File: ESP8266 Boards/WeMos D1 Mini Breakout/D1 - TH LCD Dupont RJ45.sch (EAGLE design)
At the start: 17 parts, among them J1 RJ45-8X, Q1 2N7000, Q2 2N7000

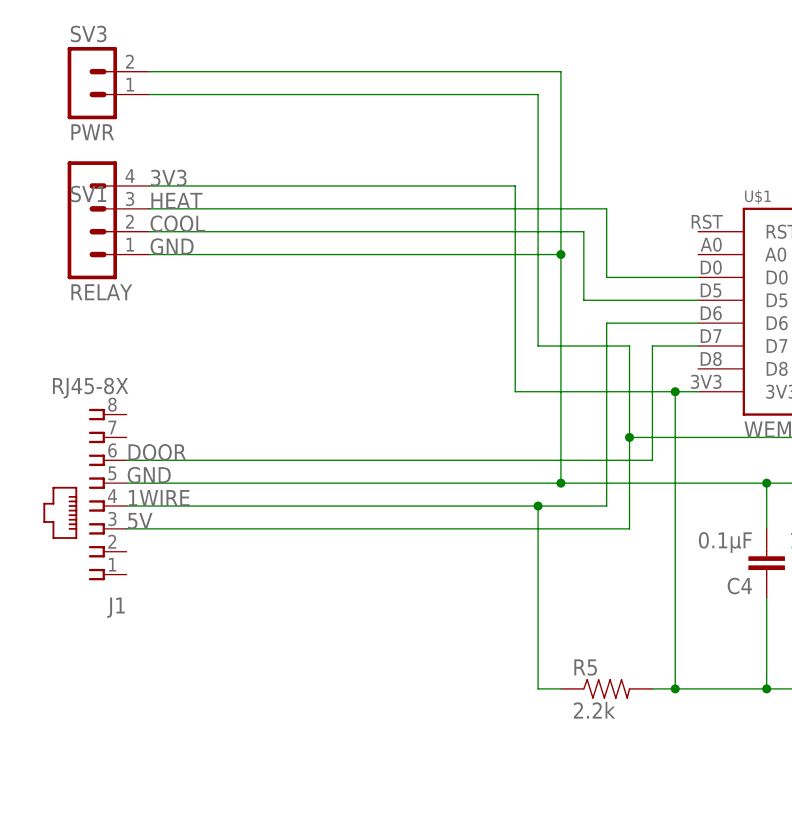
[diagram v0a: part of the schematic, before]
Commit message: Add voltage select header
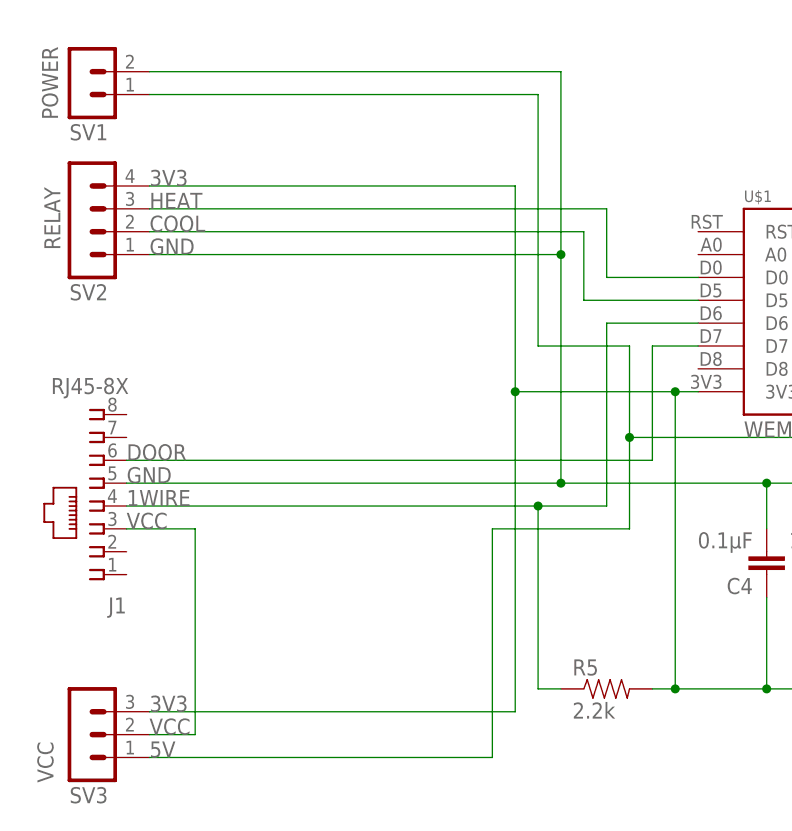
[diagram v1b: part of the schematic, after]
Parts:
- added VCC: SV3, con-lstb:MA03-1
- POWER: value PWR -> SV1
- RELAY: value RELAY -> SV2
- renumbered SV1 to RELAY, SV3 to POWER
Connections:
- new net VCC: J1.3, VCC.2
- net 3V3: now also VCC.3
- net 5V: now also VCC.1; no longer J1.3
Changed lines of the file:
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@@
 <?xml version="1.0" encoding="utf-8"?>
 <!DOCTYPE eagle SYSTEM "eagle.dtd">
-<eagle version="9.5.2">
+<eagle version="9.6.2">
 <drawing>
 <settings>
@@
 <part name="J1" library="con-tycoelectronics" deviceset="RJ45" device="" technology="-8X"/>
 <part name="R5" library="SparkFun-Resistors" library_urn="urn:adsk.eagle:library:532" deviceset="10KOHM" device="-HORIZ-1/4W-1%" package3d_urn="urn:adsk.eagle:package:39658/1" value="2.2k"/>
-<part name="SV1" library="Donnie" deviceset="HDR-4" device="" value="RELAY"/>
+<part name="RELAY" library="Donnie" deviceset="HDR-4" device="" value="SV2"/>
 <part name="SV2" library="Donnie" deviceset="HDR-4" device="" value="LCD"/>
 <part name="R3" library="SparkFun-Resistors" library_urn="urn:adsk.eagle:library:532" deviceset="10KOHM" device="-HORIZ-1/4W-1%" package3d_urn="urn:adsk.eagle:package:39658/1" value="10k"/>
@@
 <part name="C3" library="Donnie" deviceset="CAP_CERAMIC_2.54" device="" value="1.0μF"/>
 <part name="C2" library="Donnie" deviceset="CAP_CERAMIC_2.54" device="" value="0.1μF"/>
-<part name="SV3" library="Donnie" deviceset="HDR-2" device="" value="PWR"/>
+<part name="POWER" library="Donnie" deviceset="HDR-2" device="" value="SV1"/>
 <part name="FRAME1" library="frames" library_urn="urn:adsk.eagle:library:229" deviceset="LETTER_L" device="" value=" "/>
+<part name="VCC" library="con-lstb" library_urn="urn:adsk.eagle:library:162" deviceset="MA03-1" device="" package3d_urn="urn:adsk.eagle:package:8339/1" value="SV3"/>
 </parts>
 <sheets>
@@
 <attribute name="VALUE" x="92.71" y="65.278" size="1.778" layer="96"/>
 </instance>
-<instance part="SV1" gate="1" x="38.1" y="116.84" smashed="yes">
+<instance part="RELAY" gate="1" x="38.1" y="116.84" smashed="yes">
 <attribute name="VALUE" x="36.83" y="111.76" size="1.778" layer="96"/>
-<attribute name="NAME" x="36.83" y="122.682" size="1.778" layer="95"/>
+<attribute name="NAME" x="35.814" y="117.348" size="1.778" layer="95" rot="R90"/>
 </instance>
 <instance part="SV2" gate="1" x="215.9" y="78.74" smashed="yes" rot="R180">
@@
 <attribute name="VALUE" x="133.096" y="85.979" size="1.778" layer="96" font="vector" rot="R180"/>
 </instance>
-<instance part="SV3" gate="G$1" x="38.1" y="134.62" smashed="yes">
+<instance part="POWER" gate="G$1" x="38.1" y="134.62" smashed="yes">
 <attribute name="VALUE" x="36.83" y="129.54" size="1.778" layer="96"/>
-<attribute name="NAME" x="36.83" y="140.462" size="1.778" layer="95"/>
+<attribute name="NAME" x="35.56" y="131.826" size="1.778" layer="95" rot="R90"/>
 </instance>
 <instance part="FRAME1" gate="G$1" x="0" y="0" smashed="yes"/>
@@
 <attribute name="SHEET" x="233.68" y="1.27" size="2.54" layer="94"/>
 <attribute name="DRAWING_NAME" x="165.1" y="19.05" size="2.54" layer="94"/>
+</instance>
+<instance part="VCC" gate="G$1" x="38.1" y="63.5" smashed="yes">
+<attribute name="VALUE" x="36.83" y="55.88" size="1.778" layer="96"/>
+<attribute name="NAME" x="35.052" y="58.166" size="1.778" layer="95" rot="R90"/>
 </instance>
 </instances>
@@
 <wire x1="198.12" y1="91.44" x2="170.18" y2="91.44" width="0.1524" layer="91"/>
 <wire x1="149.86" y1="91.44" x2="139.7" y2="91.44" width="0.1524" layer="91"/>
-<pinref part="SV1" gate="1" pin="1"/>
+<pinref part="RELAY" gate="1" pin="1"/>
 <wire x1="45.72" y1="116.84" x2="91.44" y2="116.84" width="0.1524" layer="91"/>
 <pinref part="SV2" gate="1" pin="1"/>
@@
 <wire x1="149.86" y1="73.66" x2="149.86" y2="91.44" width="0.1524" layer="91"/>
 <junction x="149.86" y="91.44"/>
-<pinref part="SV3" gate="G$1" pin="2"/>
+<pinref part="POWER" gate="G$1" pin="2"/>
 <wire x1="45.72" y1="137.16" x2="91.44" y2="137.16" width="0.1524" layer="91"/>
 <wire x1="91.44" y1="137.16" x2="91.44" y2="116.84" width="0.1524" layer="91"/>
@@
 <label x="200.66" y="76.2" size="1.778" layer="95"/>
 <label x="165.1" y="66.04" size="1.778" layer="95" align="bottom-right"/>
-<pinref part="J1" gate="G$1" pin="3"/>
-<wire x1="43.18" y1="86.36" x2="99.06" y2="86.36" width="0.1524" layer="91"/>
-<label x="43.18" y="86.36" size="1.778" layer="95"/>
 <pinref part="C2" gate="G$1" pin="2"/>
+<wire x1="83.82" y1="86.36" x2="99.06" y2="86.36" width="0.1524" layer="91"/>
 <wire x1="134.62" y1="86.36" x2="134.62" y2="96.52" width="0.1524" layer="91"/>
-<pinref part="SV3" gate="G$1" pin="1"/>
+<pinref part="POWER" gate="G$1" pin="1"/>
 <wire x1="88.9" y1="134.62" x2="45.72" y2="134.62" width="0.1524" layer="91"/>
+<wire x1="83.82" y1="86.36" x2="83.82" y2="60.96" width="0.1524" layer="91"/>
+<pinref part="VCC" gate="G$1" pin="1"/>
+<wire x1="83.82" y1="60.96" x2="45.72" y2="60.96" width="0.1524" layer="91"/>
+<label x="45.72" y="60.96" size="1.778" layer="95"/>
 </segment>
 </net>
@@
 <junction x="104.14" y="101.6"/>
 <wire x1="86.36" y1="101.6" x2="86.36" y2="124.46" width="0.1524" layer="91"/>
-<pinref part="SV1" gate="1" pin="4"/>
+<pinref part="RELAY" gate="1" pin="4"/>
 <wire x1="86.36" y1="124.46" x2="45.72" y2="124.46" width="0.1524" layer="91"/>
 <label x="45.72" y="124.46" size="1.778" layer="95"/>
+<junction x="86.36" y="101.6"/>
+<pinref part="VCC" gate="G$1" pin="3"/>
+<wire x1="86.36" y1="66.04" x2="86.36" y2="101.6" width="0.1524" layer="91"/>
+<wire x1="45.72" y1="66.04" x2="86.36" y2="66.04" width="0.1524" layer="91"/>
+<label x="45.72" y="66.04" size="1.778" layer="95"/>
 </segment>
 </net>
@@
 <net name="COOL" class="0">
 <segment>
-<pinref part="SV1" gate="1" pin="2"/>
+<pinref part="RELAY" gate="1" pin="2"/>
 <wire x1="45.72" y1="119.38" x2="93.98" y2="119.38" width="0.1524" layer="91"/>
 <wire x1="93.98" y1="119.38" x2="93.98" y2="111.76" width="0.1524" layer="91"/>
@@
 <net name="HEAT" class="0">
 <segment>
-<pinref part="SV1" gate="1" pin="3"/>
+<pinref part="RELAY" gate="1" pin="3"/>
 <wire x1="45.72" y1="121.92" x2="96.52" y2="121.92" width="0.1524" layer="91"/>
 <wire x1="96.52" y1="121.92" x2="96.52" y2="114.3" width="0.1524" layer="91"/>
@@
 </segment>
 </net>
+<net name="VCC" class="0">
+<segment>
+<pinref part="J1" gate="G$1" pin="3"/>
+<wire x1="43.18" y1="86.36" x2="50.8" y2="86.36" width="0.1524" layer="91"/>
+<wire x1="50.8" y1="86.36" x2="50.8" y2="63.5" width="0.1524" layer="91"/>
+<pinref part="VCC" gate="G$1" pin="2"/>
+<wire x1="50.8" y1="63.5" x2="45.72" y2="63.5" width="0.1524" layer="91"/>
+<label x="43.18" y="86.36" size="1.778" layer="95"/>
+<label x="45.72" y="63.5" size="1.778" layer="95"/>
+</segment>
+</net>

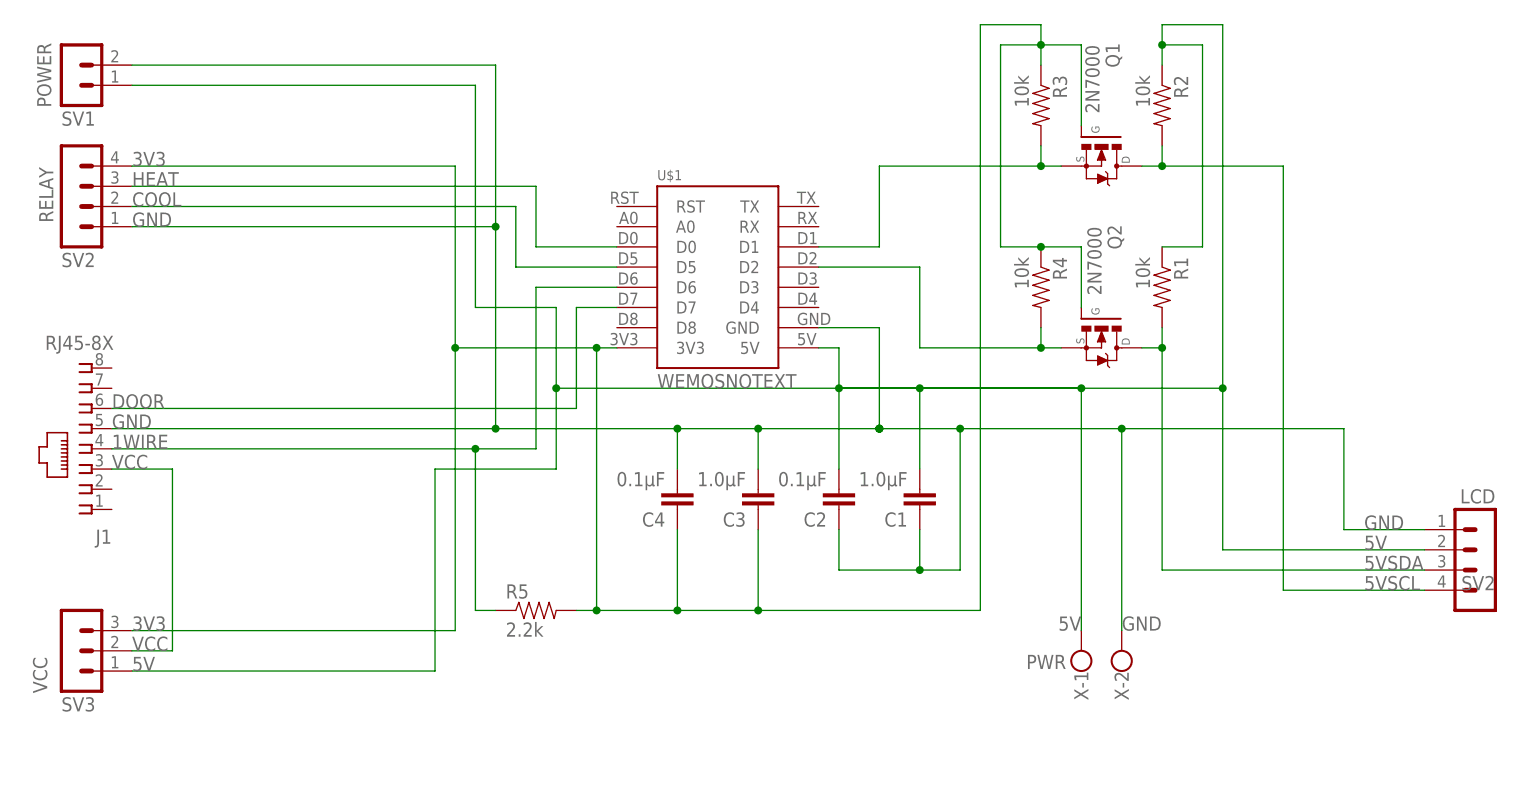
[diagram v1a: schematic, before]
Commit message: Fix pour and links
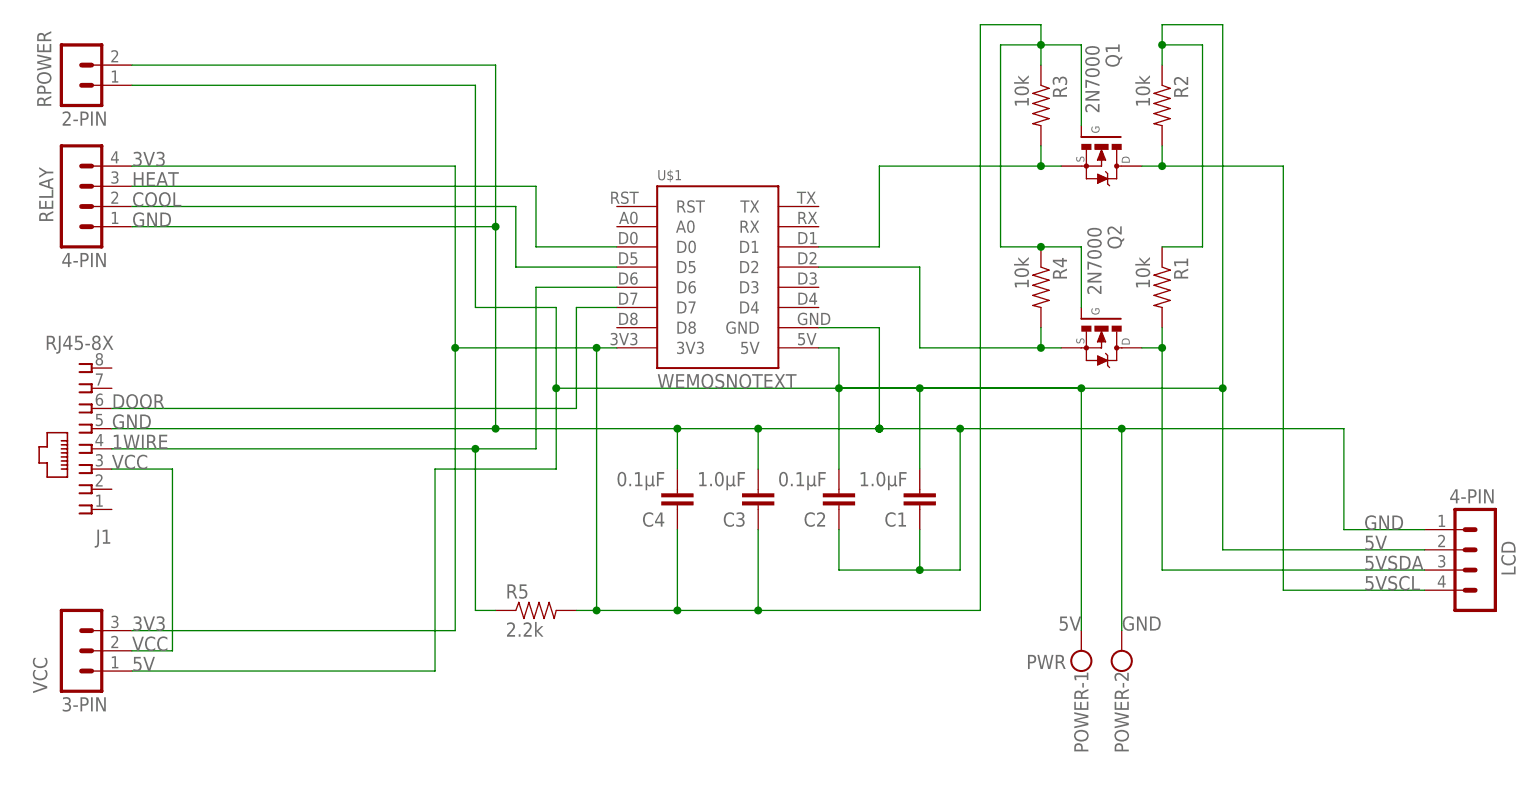
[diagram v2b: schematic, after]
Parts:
- removed X: PWR, con-wago-500:W237-102
- added RPOWER: 2-PIN, Donnie:HDR-2
- LCD: value LCD -> 4-PIN
- POWER: value SV1 -> PWR; device Donnie:HDR-2 -> con-wago-500:W237-102
- RELAY: value SV2 -> 4-PIN
- VCC: value SV3 -> 3-PIN
- renumbered SV2 to LCD
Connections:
- net 5V: now also POWER-1.KL, RPOWER.1; no longer POWER.1, X-1.KL
- net GND: now also POWER-2.KL, RPOWER.2; no longer POWER.2, X-2.KL
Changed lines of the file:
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@@
 <parts>
 <part name="U$1" library="Wemos" deviceset="WEMOS" device="NOTEXT"/>
-<part name="X" library="con-wago-500" deviceset="W237-102" device="" value="PWR"/>
+<part name="POWER" library="con-wago-500" deviceset="W237-102" device="" value="PWR"/>
 <part name="J1" library="con-tycoelectronics" deviceset="RJ45" device="" technology="-8X"/>
 <part name="R5" library="SparkFun-Resistors" library_urn="urn:adsk.eagle:library:532" deviceset="10KOHM" device="-HORIZ-1/4W-1%" package3d_urn="urn:adsk.eagle:package:39658/1" value="2.2k"/>
-<part name="RELAY" library="Donnie" deviceset="HDR-4" device="" value="SV2"/>
-<part name="SV2" library="Donnie" deviceset="HDR-4" device="" value="LCD"/>
+<part name="RELAY" library="Donnie" deviceset="HDR-4" device="" value="4-PIN"/>
+<part name="LCD" library="Donnie" deviceset="HDR-4" device="" value="4-PIN"/>
 <part name="R3" library="SparkFun-Resistors" library_urn="urn:adsk.eagle:library:532" deviceset="10KOHM" device="-HORIZ-1/4W-1%" package3d_urn="urn:adsk.eagle:package:39658/1" value="10k"/>
 <part name="R2" library="SparkFun-Resistors" library_urn="urn:adsk.eagle:library:532" deviceset="10KOHM" device="-HORIZ-1/4W-1%" package3d_urn="urn:adsk.eagle:package:39658/1" value="10k"/>
@@
 <part name="C3" library="Donnie" deviceset="CAP_CERAMIC_2.54" device="" value="1.0μF"/>
 <part name="C2" library="Donnie" deviceset="CAP_CERAMIC_2.54" device="" value="0.1μF"/>
-<part name="POWER" library="Donnie" deviceset="HDR-2" device="" value="SV1"/>
+<part name="RPOWER" library="Donnie" deviceset="HDR-2" device="" value="2-PIN"/>
 <part name="FRAME1" library="frames" library_urn="urn:adsk.eagle:library:229" deviceset="LETTER_L" device="" value=" "/>
-<part name="VCC" library="con-lstb" library_urn="urn:adsk.eagle:library:162" deviceset="MA03-1" device="" package3d_urn="urn:adsk.eagle:package:8339/1" value="SV3"/>
+<part name="VCC" library="con-lstb" library_urn="urn:adsk.eagle:library:162" deviceset="MA03-1" device="" package3d_urn="urn:adsk.eagle:package:8339/1" value="3-PIN"/>
 </parts>
 <sheets>
@@
 <attribute name="VALUE" x="111.76" y="96.52" size="1.778" layer="96"/>
 </instance>
-<instance part="X" gate="-1" x="165.1" y="60.96" smashed="yes" rot="R90">
+<instance part="POWER" gate="-1" x="165.1" y="60.96" smashed="yes" rot="R90">
 <attribute name="NAME" x="164.211" y="60.96" size="1.778" layer="95" rot="R270"/>
 </instance>
-<instance part="X" gate="-2" x="170.18" y="60.96" smashed="yes" rot="R90">
+<instance part="POWER" gate="-2" x="170.18" y="60.96" smashed="yes" rot="R90">
 <attribute name="VALUE" x="163.195" y="62.992" size="1.778" layer="96" rot="R180"/>
 <attribute name="NAME" x="169.291" y="60.96" size="1.778" layer="95" rot="R270"/>
@@
 <attribute name="NAME" x="35.814" y="117.348" size="1.778" layer="95" rot="R90"/>
 </instance>
-<instance part="SV2" gate="1" x="215.9" y="78.74" smashed="yes" rot="R180">
+<instance part="LCD" gate="1" x="215.9" y="78.74" smashed="yes" rot="R180">
 <attribute name="VALUE" x="217.17" y="83.82" size="1.778" layer="96" rot="R180"/>
-<attribute name="NAME" x="217.17" y="72.898" size="1.778" layer="95" rot="R180"/>
+<attribute name="NAME" x="219.71" y="72.898" size="1.778" layer="95" rot="R90"/>
 </instance>
 <instance part="R3" gate="G$1" x="160.02" y="132.08" smashed="yes" rot="R270">
@@
 <attribute name="VALUE" x="133.096" y="85.979" size="1.778" layer="96" font="vector" rot="R180"/>
 </instance>
-<instance part="POWER" gate="G$1" x="38.1" y="134.62" smashed="yes">
+<instance part="RPOWER" gate="G$1" x="38.1" y="134.62" smashed="yes">
 <attribute name="VALUE" x="36.83" y="129.54" size="1.778" layer="96"/>
 <attribute name="NAME" x="35.56" y="131.826" size="1.778" layer="95" rot="R90"/>
@@
 <pinref part="U$1" gate="G$1" pin="GND"/>
 <wire x1="132.08" y1="104.14" x2="139.7" y2="104.14" width="0.1524" layer="91"/>
-<pinref part="X" gate="-2" pin="KL"/>
+<pinref part="POWER" gate="-2" pin="KL"/>
 <wire x1="170.18" y1="66.04" x2="170.18" y2="91.44" width="0.1524" layer="91"/>
 <junction x="170.18" y="91.44"/>
@@
 <pinref part="RELAY" gate="1" pin="1"/>
 <wire x1="45.72" y1="116.84" x2="91.44" y2="116.84" width="0.1524" layer="91"/>
-<pinref part="SV2" gate="1" pin="1"/>
+<pinref part="LCD" gate="1" pin="1"/>
 <pinref part="C1" gate="G$1" pin="1"/>
 <junction x="139.7" y="91.44"/>
@@
 <wire x1="149.86" y1="73.66" x2="149.86" y2="91.44" width="0.1524" layer="91"/>
 <junction x="149.86" y="91.44"/>
-<pinref part="POWER" gate="G$1" pin="2"/>
+<pinref part="RPOWER" gate="G$1" pin="2"/>
 <wire x1="45.72" y1="137.16" x2="91.44" y2="137.16" width="0.1524" layer="91"/>
 <wire x1="91.44" y1="137.16" x2="91.44" y2="116.84" width="0.1524" layer="91"/>
@@
 <wire x1="134.62" y1="101.6" x2="134.62" y2="96.52" width="0.1524" layer="91"/>
 <wire x1="134.62" y1="96.52" x2="165.1" y2="96.52" width="0.1524" layer="91"/>
-<pinref part="X" gate="-1" pin="KL"/>
+<pinref part="POWER" gate="-1" pin="KL"/>
 <wire x1="165.1" y1="66.04" x2="165.1" y2="96.52" width="0.1524" layer="91"/>
 <wire x1="165.1" y1="96.52" x2="144.78" y2="96.52" width="0.1524" layer="91"/>
@@
 <wire x1="182.88" y1="76.2" x2="182.88" y2="96.52" width="0.1524" layer="91"/>
 <wire x1="88.9" y1="106.68" x2="88.9" y2="134.62" width="0.1524" layer="91"/>
-<pinref part="SV2" gate="1" pin="2"/>
+<pinref part="LCD" gate="1" pin="2"/>
 <pinref part="C1" gate="G$1" pin="2"/>
 <wire x1="144.78" y1="86.36" x2="144.78" y2="96.52" width="0.1524" layer="91"/>
@@
 <wire x1="83.82" y1="86.36" x2="99.06" y2="86.36" width="0.1524" layer="91"/>
 <wire x1="134.62" y1="86.36" x2="134.62" y2="96.52" width="0.1524" layer="91"/>
-<pinref part="POWER" gate="G$1" pin="1"/>
+<pinref part="RPOWER" gate="G$1" pin="1"/>
 <wire x1="88.9" y1="134.62" x2="45.72" y2="134.62" width="0.1524" layer="91"/>
 <wire x1="83.82" y1="86.36" x2="83.82" y2="60.96" width="0.1524" layer="91"/>
@@
 <net name="5VSCL" class="0">
 <segment>
-<pinref part="SV2" gate="1" pin="4"/>
+<pinref part="LCD" gate="1" pin="4"/>
 <wire x1="208.28" y1="71.12" x2="190.5" y2="71.12" width="0.1524" layer="91"/>
 <wire x1="190.5" y1="71.12" x2="190.5" y2="124.46" width="0.1524" layer="91"/>
@@
 <segment>
 <wire x1="208.28" y1="73.66" x2="175.26" y2="73.66" width="0.1524" layer="91"/>
-<pinref part="SV2" gate="1" pin="3"/>
+<pinref part="LCD" gate="1" pin="3"/>
 <wire x1="175.26" y1="73.66" x2="175.26" y2="101.6" width="0.1524" layer="91"/>
 <pinref part="R1" gate="G$1" pin="2"/>
